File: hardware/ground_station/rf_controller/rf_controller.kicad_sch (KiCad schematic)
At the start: 58 parts, among them J1 USB_C_Receptacle_USB2.0_16P, J1-3V3 Conn_01x02, J2-MCU1 Conn_01x02, J8-L62 Conn_01x02, J9-L80 Conn_01x02, U1 LDL112PV33R, Y1 16MHz

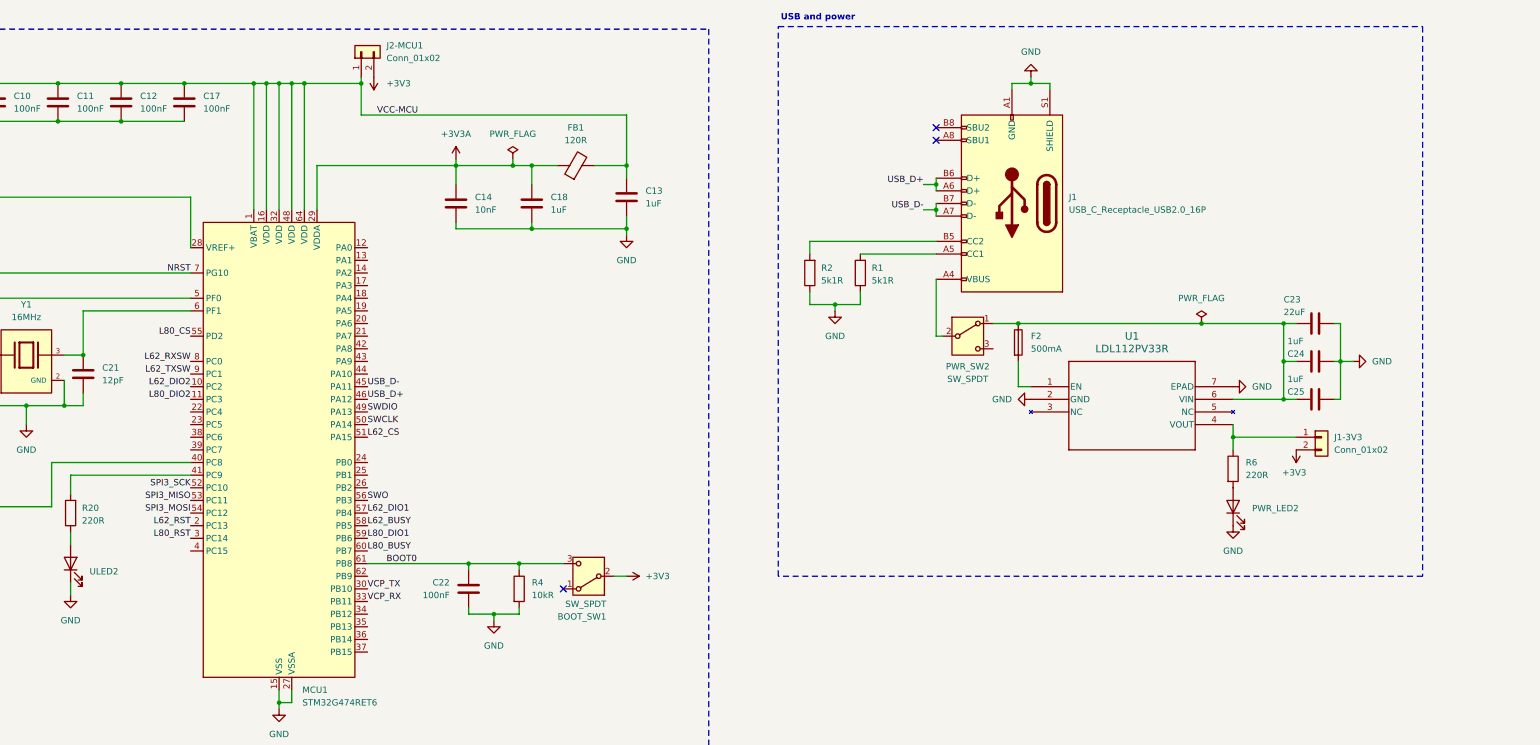
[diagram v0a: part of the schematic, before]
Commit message: PCB layout for RF controller And additional updates to schematic: - Added ESD protection to USB data lines - Fixed wrong placement of capacitors around LDO voltage regulator - Added extra user LED and button
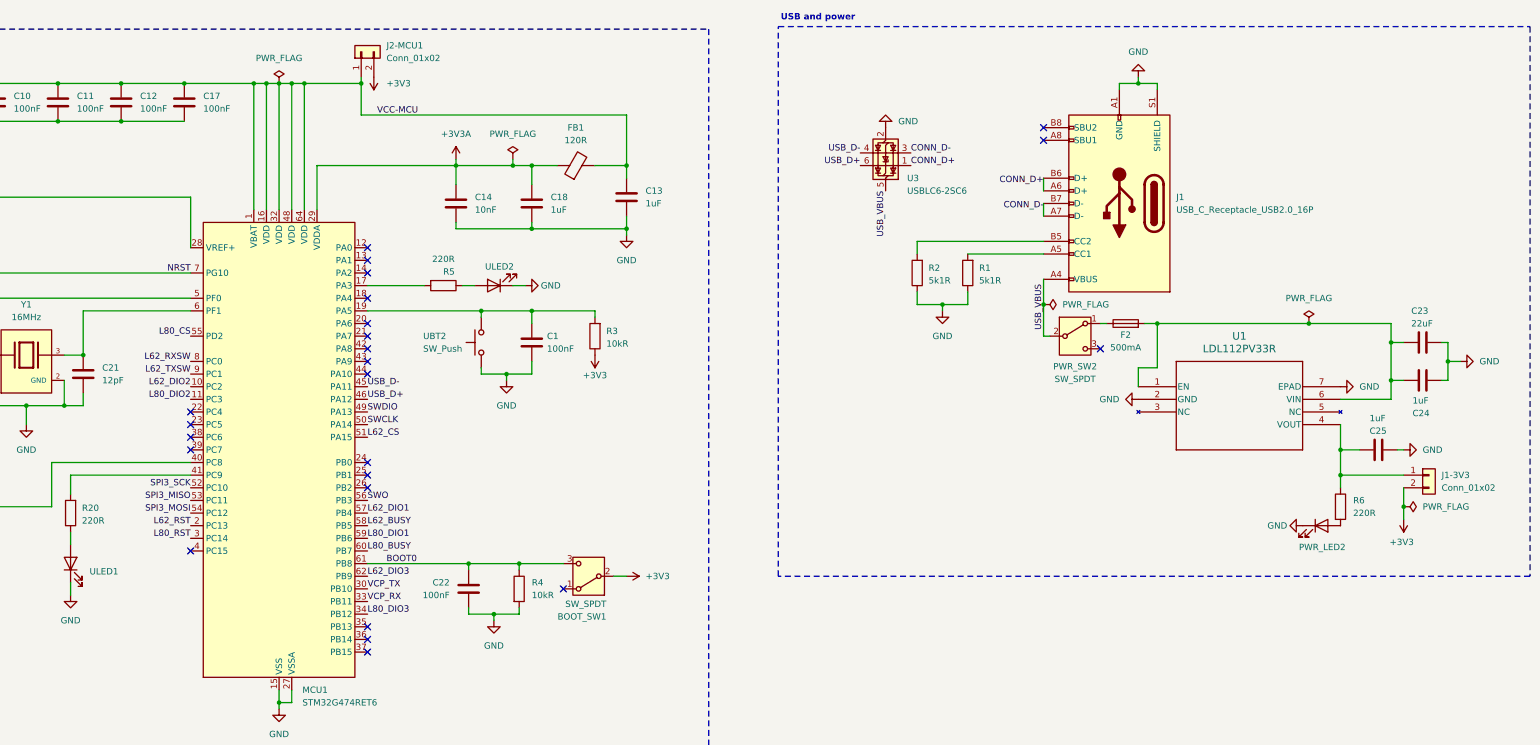
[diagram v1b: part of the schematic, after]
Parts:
- added C1: 100nF, Capacitor_SMD:C_0603_1608Metric, symbol Device:C
- added R3: 10kR, Resistor_SMD:R_0603_1608Metric, symbol Device:R
- added R5: 220R, Resistor_SMD:R_0603_1608Metric, symbol Device:R
- added U3: USBLC6-2SC6, Package_TO_SOT_SMD:SOT-23-6, symbol Power_Protection:USBLC6-2SC6
- added UBT2: SW_Push, avionicsw:hanxia HX 3x4x2-2P-1.6N TACTILE SWITCH, symbol Switch:SW_Push
- added ULED2: PWR LED, LED_SMD:LED_0805_2012Metric, symbol Device:LED
- renumbered ULED2 to ULED1
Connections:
- net +3V3: now also R3.1
- net GND: now also C1.2, U3.2 (GND), UBT2.1, ULED2.1 (K)
- net L62_DIO3: now also MCU1.62 (PB9)
- net L80_DIO3: now also MCU1.34 (PB12)
- net USB_D+: now also U3.6 (I/O1); no longer J1.A6 (D+), J1.B6 (D+)
- net USB_D-: now also U3.4 (I/O2); no longer J1.A7 (D-), J1.B7 (D-)
- net USB_VBUS: now reaches J1.A4 (VBUS), J1.A9 (VBUS), J1.B4 (VBUS), J1.B9 (VBUS), PWR_SW2.2 (B)
- net USB_VBUS: now also U3.5 (VBUS)
- net at J1-3V3.1 (Pin_1), R6.1, U1.4 (VOUT): now also C25.1
- net at C23.1, C24.1, U1.6 (VIN): now also F2.2, U1.1 (EN); no longer C25.1, F2.1, PWR_SW2.1 (A)
- net at MCU1.17 (PA3): now also R5.2
- net at MCU1.19 (PA5): now also C1.1, R3.2, UBT2.2
- new net: R5.1, ULED2.2 (A)
- new net: F2.1, PWR_SW2.1 (A)
- new net CONN_D+: J1.A6 (D+), J1.B6 (D+), U3.1 (I/O1)
- new net CONN_D-: J1.A7 (D-), J1.B7 (D-), U3.3 (I/O2)
- no-connect marks 13 -> 34
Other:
- moved on the sheet: C23, C24, C25, F2, J1, J1-3V3, PWR_LED2, PWR_SW2, R1, R2, R6, U1

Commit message: Finalised RF controller PCB layout
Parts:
- removed H4: MountingHole, MountingHole:MountingHole_2.2mm_M2, symbol Mechanical:MountingHole
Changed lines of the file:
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@@
-	)
-	(symbol
-		(lib_id "Mechanical:MountingHole")
-		(at 417.83 364.49 0)
-		(unit 1)
-		(exclude_from_sim no)
-		(in_bom no)
-		(on_board yes)
-		(dnp no)
-		(fields_autoplaced yes)
-		(property "Reference" "H4"
-			(at 420.37 363.2199 0)
-			(effects
-				(font
-					(size 1.27 1.27)
-				)
-				(justify left)
-			)
-		)
-		(property "Value" "MountingHole"
-			(at 420.37 365.7599 0)
-			(effects
-				(font
-					(size 1.27 1.27)
-				)
-				(justify left)
-			)
-		)
-		(property "Footprint" "MountingHole:MountingHole_2.2mm_M2"
-			(at 417.83 364.49 0)
-			(effects
-				(font
-					(size 1.27 1.27)
-				)
-				(hide yes)
-			)
-		)
-		(property "Datasheet" "~"
-			(at 417.83 364.49 0)
-			(effects
-				(font
-					(size 1.27 1.27)
-				)
-				(hide yes)
-			)
-		)
-		(property "Description" "Mounting Hole without connection"
-			(at 417.83 364.49 0)
-			(effects
-				(font
-					(size 1.27 1.27)
-				)
-				(hide yes)
-			)
-		)
-		(instances
-			(project "rf_controller"
-				(path "/01dafd25-96fd-4782-8847-6537a2ab82e1"
-					(reference "H4")
-					(unit 1)
-				)
-			)
-		)
 	)
 	(symbol
